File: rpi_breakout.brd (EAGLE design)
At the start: 35.6 x 35.6 mm, 26 parts, among them U2 TXB0108, U3 TXB0108

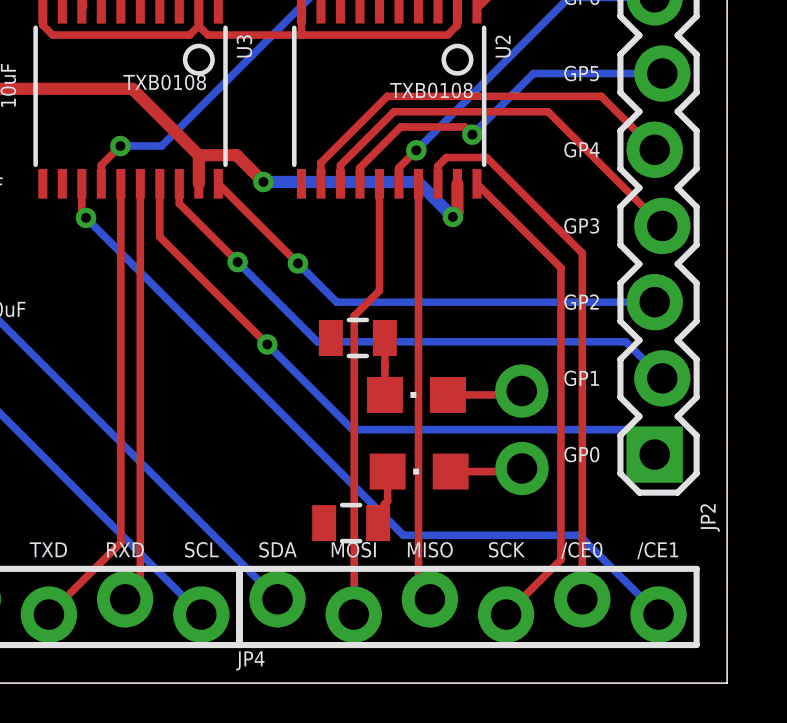
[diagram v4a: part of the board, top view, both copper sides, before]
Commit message: Line up the blinkenpins on a 0.1" grid
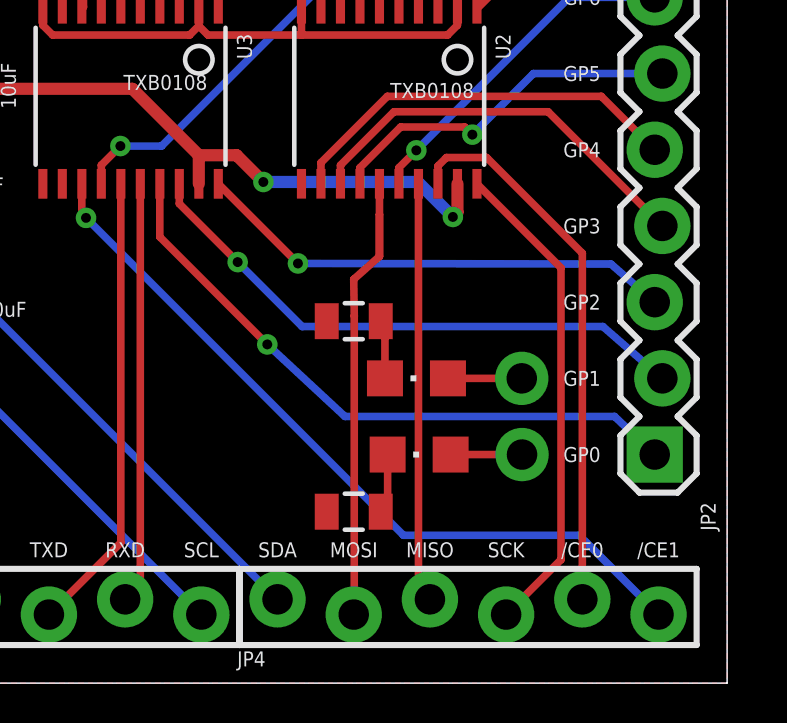
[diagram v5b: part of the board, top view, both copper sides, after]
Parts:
- moved R3 0.57 mm to (23.1, 12.1)
- moved LED4 0.57 mm to (25.3, 7.62)
- moved LED3 0.55 mm to (25.2, 10.2)
- moved JP8 0.46 mm to (28.7, 7.62)
- moved JP7 0.42 mm to (28.7, 10.2)
- moved R4 0.39 mm to (23.1, 5.71)
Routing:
- net SPI_MOSIV: track 14.7 -> 16.1 mm
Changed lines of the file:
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@@
 <element name="LED1" library="adafruit" package="CHIPLED_0805" value="CONNECTED" x="9.6685" y="7.8693" smashed="yes" rot="R270"/>
 <element name="LED2" library="adafruit" package="CHIPLED_0805" value="IO-POWER" x="9.6488" y="5.3643" smashed="yes" rot="R270"/>
-<element name="R3" library="SparkFun" package="0805" value="330" x="23.2506" y="11.5067" smashed="yes" rot="R180"/>
-<element name="LED3" library="adafruit" package="CHIPLED_0805" value="BLINKY" x="25.2045" y="9.6068" smashed="yes" rot="R90"/>
-<element name="JP7" library="adafruit" package="1X01-CLEANBIG" value="LED3" x="28.7156" y="9.7367" smashed="yes"/>
-<element name="R4" library="SparkFun" package="0805" value="330" x="23.0282" y="5.335" smashed="yes" rot="R180"/>
-<element name="LED4" library="adafruit" package="CHIPLED_0805" value="BLINKY" x="25.2945" y="7.0527" smashed="yes" rot="R90"/>
-<element name="JP8" library="adafruit" package="1X01-CLEANBIG" value="LED4" x="28.7239" y="7.156" smashed="yes"/>
+<element name="R3" library="SparkFun" package="0805" value="330" x="23.114" y="12.065" smashed="yes" rot="R180"/>
+<element name="LED3" library="adafruit" package="CHIPLED_0805" value="BLINKY" x="25.2045" y="10.16" smashed="yes" rot="R90"/>
+<element name="JP7" library="adafruit" package="1X01-CLEANBIG" value="LED3" x="28.7156" y="10.16" smashed="yes"/>
+<element name="R4" library="SparkFun" package="0805" value="330" x="23.114" y="5.715" smashed="yes" rot="R180"/>
+<element name="LED4" library="adafruit" package="CHIPLED_0805" value="BLINKY" x="25.2945" y="7.62" smashed="yes" rot="R90"/>
+<element name="JP8" library="adafruit" package="1X01-CLEANBIG" value="LED4" x="28.7239" y="7.62" smashed="yes"/>
 <element name="U3" library="rpi_breakout" package="TSSOP20" value="TXB0108" x="15.6752" y="19.5621" smashed="yes" rot="R180">
 <attribute name="NAME" x="19.2208" y="21.6449" size="0.5" layer="21" font="vector" rot="R270"/>
@@
 <wire x1="16.6502" y1="16.6443" x2="16.6502" y2="14.8737" width="0.254" layer="1"/>
 <wire x1="16.6502" y1="14.8737" x2="20.2325" y2="11.2914" width="0.254" layer="1"/>
-<wire x1="33.147" y1="7.62" x2="32.3165" y2="8.4505" width="0.254" layer="16"/>
-<wire x1="32.3165" y1="8.4505" x2="23.0734" y2="8.4505" width="0.254" layer="16"/>
-<wire x1="23.0734" y1="8.4505" x2="20.2325" y2="11.2914" width="0.254" layer="16"/>
+<wire x1="33.147" y1="7.62" x2="31.8085" y2="8.89" width="0.254" layer="16"/>
+<wire x1="31.8085" y1="8.89" x2="22.8194" y2="8.89" width="0.254" layer="16"/>
+<wire x1="22.8194" y1="8.89" x2="20.2325" y2="11.2914" width="0.254" layer="16"/>
 <via x="20.2325" y="11.2914" extent="1-16" drill="0.3302" diameter="0.6858"/>
 </signal>
@@
 <wire x1="17.3002" y1="16.6443" x2="17.3002" y2="15.9804" width="0.254" layer="1"/>
 <wire x1="17.3002" y1="15.9804" x2="19.2448" y2="14.0358" width="0.254" layer="1"/>
-<wire x1="33.401" y1="10.16" x2="32.182" y2="11.379" width="0.254" layer="16"/>
-<wire x1="32.182" y1="11.379" x2="21.9016" y2="11.379" width="0.254" layer="16"/>
-<wire x1="21.9016" y1="11.379" x2="19.2448" y2="14.0358" width="0.254" layer="16"/>
+<wire x1="33.401" y1="10.16" x2="31.42" y2="11.887" width="0.254" layer="16"/>
+<wire x1="31.42" y1="11.887" x2="21.3936" y2="11.887" width="0.254" layer="16"/>
+<wire x1="21.3936" y1="11.887" x2="19.2448" y2="14.0358" width="0.254" layer="16"/>
 <via x="19.2448" y="14.0358" extent="1-16" drill="0.3302" diameter="0.6858"/>
 </signal>
@@
 <wire x1="18.6002" y1="16.6443" x2="21.2544" y2="13.9901" width="0.254" layer="1"/>
 <wire x1="21.2544" y1="13.9901" x2="21.2547" y2="13.9901" width="0.254" layer="1"/>
-<wire x1="33.147" y1="12.7" x2="22.5448" y2="12.7" width="0.254" layer="16"/>
-<wire x1="22.5448" y1="12.7" x2="21.2547" y2="13.9901" width="0.254" layer="16"/>
+<wire x1="33.147" y1="12.7" x2="31.6888" y2="13.97" width="0.254" layer="16"/>
+<wire x1="31.6888" y1="13.97" x2="21.2547" y2="13.9901" width="0.254" layer="16"/>
 <via x="21.2547" y="13.9901" extent="1-16" drill="0.3302" diameter="0.6858"/>
 </signal>
@@
 <contactref element="JP7" pad="1"/>
 <contactref element="LED3" pad="A"/>
-<wire x1="26.2545" y1="9.6068" x2="28.5857" y2="9.6068" width="0.254" layer="1"/>
-<wire x1="28.5857" y1="9.6068" x2="28.7156" y2="9.7367" width="0.254" layer="1"/>
+<wire x1="26.2545" y1="10.16" x2="28.7156" y2="10.16" width="0.254" layer="1"/>
 </signal>
 <signal name="LED4_JP">
 <contactref element="JP8" pad="1"/>
 <contactref element="LED4" pad="A"/>
-<wire x1="26.3445" y1="7.0527" x2="28.6206" y2="7.0527" width="0.254" layer="1"/>
-<wire x1="28.6206" y1="7.0527" x2="28.7239" y2="7.156" width="0.254" layer="1"/>
+<wire x1="28.7239" y1="7.62" x2="26.3445" y2="7.62" width="0.254" layer="1"/>
 </signal>
 <signal name="RXDV">
@@
 <wire x1="23.114" y1="2.286" x2="23.1317" y2="2.3037" width="0.254" layer="1"/>
 <wire x1="23.1317" y1="2.3037" x2="23.1317" y2="12.2411" width="0.254" layer="1"/>
-<wire x1="23.1317" y1="12.2411" x2="23.9718" y2="13.0812" width="0.254" layer="1"/>
-<wire x1="23.9718" y1="13.0812" x2="23.9718" y2="16.6447" width="0.254" layer="1"/>
+<wire x1="23.9718" y1="15.6212" x2="23.9718" y2="14.224" width="0.254" layer="1"/>
+<wire x1="23.9718" y1="14.224" x2="23.9718" y2="15.6212" width="0.254" layer="1"/>
+<wire x1="23.9718" y1="15.6212" x2="23.9718" y2="16.6447" width="0.254" layer="1"/>
+<wire x1="23.1317" y1="12.2411" x2="23.114" y2="13.462" width="0.254" layer="1"/>
+<wire x1="23.114" y1="13.462" x2="23.9718" y2="14.224" width="0.254" layer="1"/>
 </signal>
 <signal name="SPI_MISOV">
@@
 <contactref element="R3" pad="1"/>
 <wire x1="24.1545" y1="10.5879" x2="24.1545" y2="11.5028" width="0.254" layer="1"/>
-<wire x1="24.1545" y1="11.5028" x2="24.1506" y2="11.5067" width="0.254" layer="1"/>
-<wire x1="24.1545" y1="9.6068" x2="24.1545" y2="10.5879" width="0.254" layer="1"/>
-<wire x1="24.1545" y1="10.0248" x2="24.1545" y2="9.6068" width="0.254" layer="1"/>
+<wire x1="24.1545" y1="11.5028" x2="24.014" y2="12.065" width="0.254" layer="1"/>
+<wire x1="24.1545" y1="10.16" x2="24.1545" y2="10.5879" width="0.254" layer="1"/>
+<wire x1="24.1545" y1="10.0248" x2="24.1545" y2="10.16" width="0.254" layer="1"/>
 </signal>
 <signal name="N$4">
 <contactref element="R4" pad="1"/>
 <contactref element="LED4" pad="C"/>
-<wire x1="24.2445" y1="7.0527" x2="24.2445" y2="6.0716" width="0.254" layer="1"/>
+<wire x1="24.2445" y1="7.62" x2="24.2445" y2="6.0716" width="0.254" layer="1"/>
 <wire x1="24.2445" y1="6.0716" x2="24.13" y2="5.9571" width="0.254" layer="1"/>
 <wire x1="24.13" y1="5.9571" x2="24.13" y2="5.588" width="0.254" layer="1"/>
-<wire x1="24.13" y1="5.588" x2="23.9282" y2="5.335" width="0.254" layer="1"/>
+<wire x1="24.13" y1="5.588" x2="24.014" y2="5.715" width="0.254" layer="1"/>
 </signal>
 <signal name="5V" class="1">
